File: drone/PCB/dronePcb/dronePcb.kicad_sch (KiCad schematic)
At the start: 19 parts, among them M1 Motor_DC, M3 Motor_DC, M4 Motor_DC, Q1 PN2222A, Q2 PN2222A, Q3 PN2222A, Q4 PN2222A, SW1 SW_DPST_x2, U1 XIAO-ESP32-C6-DIP

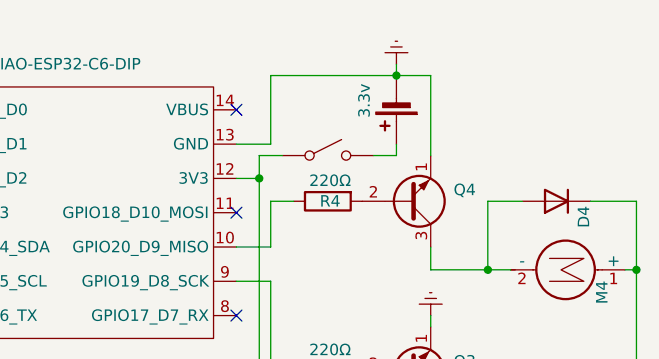
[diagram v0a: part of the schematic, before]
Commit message: modify ecr error
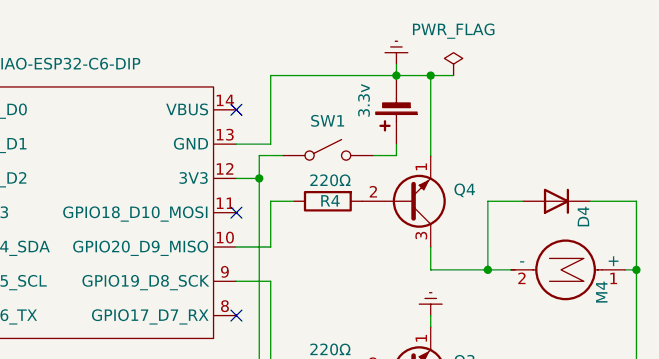
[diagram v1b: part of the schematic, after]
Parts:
- removed SW1: SW_DPST_x2, symbol Switch:SW_DPST_x2
- added SW1: SW_SPST, symbol Switch:SW_SPST
- M2: value ~ -> (none)
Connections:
- net at D1.1 (K), D2.1 (K), D3.1 (K)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: now also SW1.1 (A)
- net at BT2.1 (+): now also SW1.2 (B)

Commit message: PCB作成エラーなし
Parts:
- removed SW1: SW_SPST, symbol Switch:SW_SPST
- added BT3: 3.3v, Connector_PinHeader_2.54mm:PinHeader_2x01_P2.54mm_Vertical, symbol Device:Battery_Cell
- added SW1, SW2: SW_Push, Button_Switch_THT:SW_PUSH_6mm, symbol Switch:SW_Push
- BT2, M1, M2, M3, M4: footprint (none) -> Connector_PinHeader_2.54mm:PinHeader_2x01_P2.54mm_Vertical
- R1, R2, R3, R4: footprint (none) -> Resistor_THT:R_Axial_DIN0207_L6.3mm_D2.5mm_P10.16mm_Horizontal
- U1: footprint Seeed_Studio_XIAO_Series:XIAO-ESP32-C6-DIP -> New_XIAO_Series_Footprints:XIAO-ESP32-C6-DIP
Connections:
- net GNDREF: now also BT3.2 (-)
- net at D1.1 (K), D2.1 (K), D3.1 (K)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: now also SW2.1; no longer U1.12 (3V3)
- net at BT2.1 (+): now also SW1.2
- new net: BT3.1 (+), SW2.2
- new net: SW1.1, U1.12 (3V3)
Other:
- moved on the sheet: D4, M4, Q4, R4
